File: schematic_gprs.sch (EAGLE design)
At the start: 46 parts, among them J1 Jumper Alimentaciones, Q1 MOSFET-NCHANNEL2N7000, Q2 MOSFET-NCHANNEL2N7000, T1 BC547, X1 LTI-SASF54GT

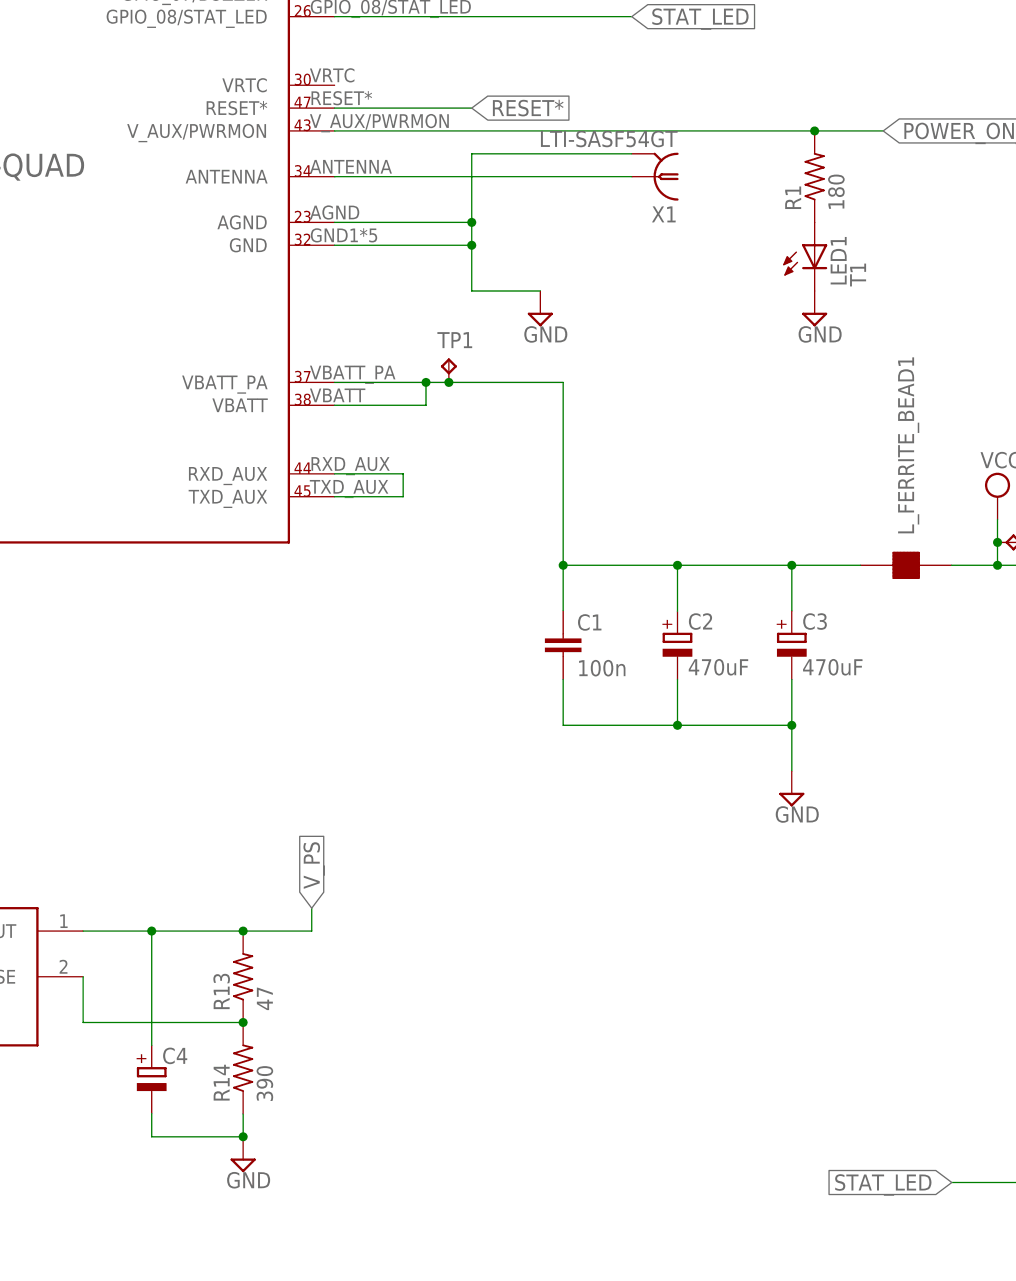
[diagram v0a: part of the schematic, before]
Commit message: Pistas realizadas
Se acaban todas las conexiones restantes. Se replantean los valores de
las resistencias para el led y se modifican también los valores de las
resistencias a la salida del regulador de tensión. Se añade un
condensador de 1uF a la entrada de VCC de la tarjeta SIM:
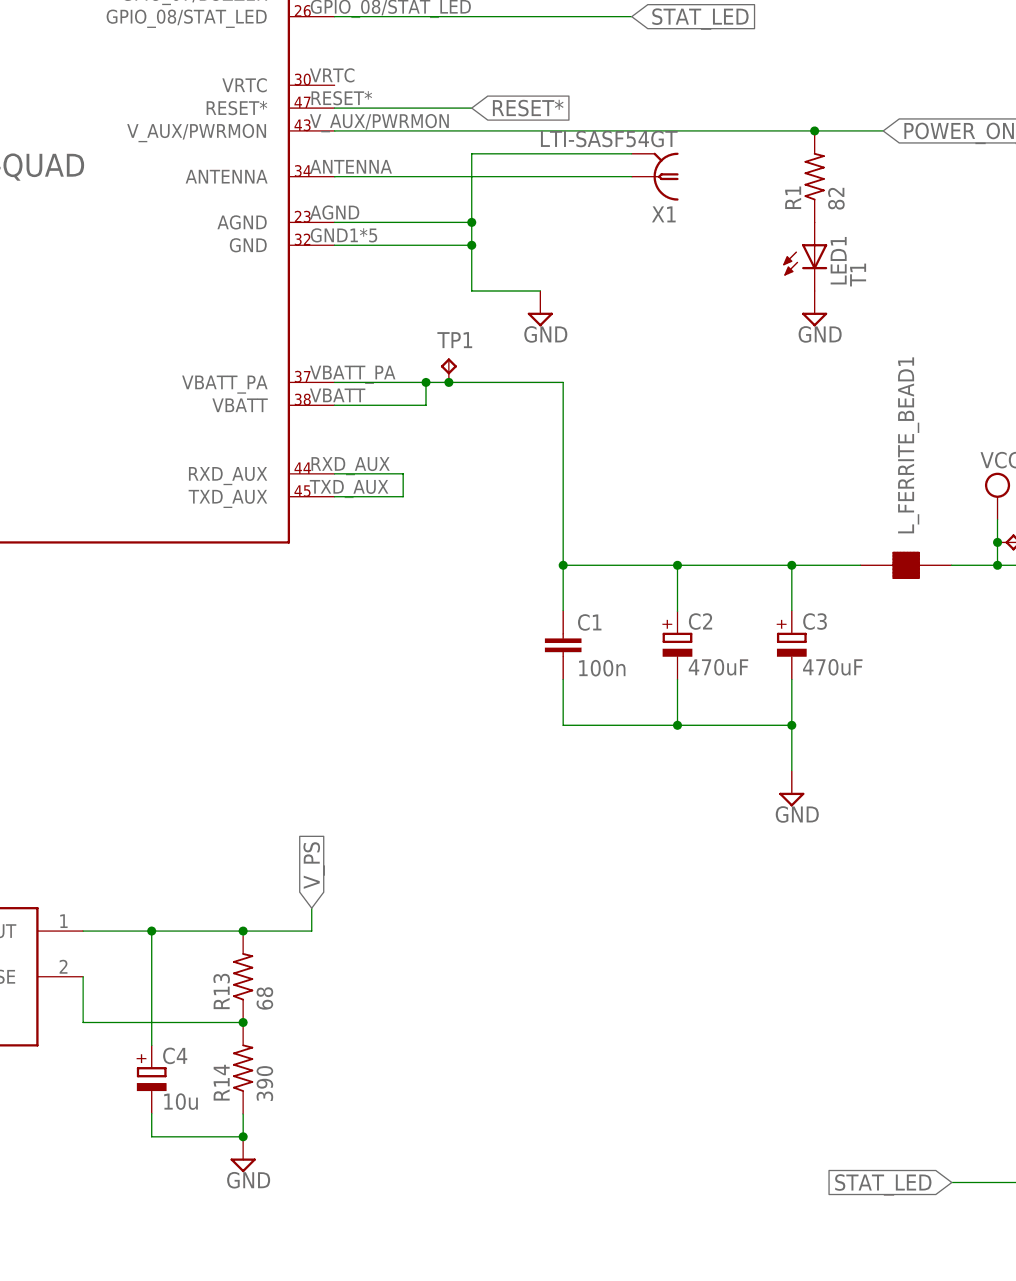
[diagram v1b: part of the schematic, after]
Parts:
- C4: value (none) -> 10u
- R1: value 180 -> 82
- R13: value 47 -> 68
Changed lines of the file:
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@@
 <part name="LED1" library="led" deviceset="LED" device="3MM" value="T1"/>
 <part name="SUPPLY10" library="supply2" deviceset="GND" device=""/>
-<part name="R1" library="resistor" deviceset="R-US_" device="0207/7" value="180"/>
+<part name="R1" library="resistor" deviceset="R-US_" device="0207/7" value="82"/>
 <part name="R3" library="resistor" deviceset="R-US_" device="0207/7" value="180"/>
 <part name="LED2" library="led" deviceset="LED" device="3MM" value="T1"/>
@@
 <part name="J1" library="jumper" deviceset="J2" device="X2MM" value="Jumper Alimentaciones"/>
 <part name="L_FERRITE_BEAD1" library="sym" deviceset="FERRITEBEAD2" device=""/>
-<part name="R13" library="resistor" deviceset="R-US_" device="0207/7" value="47"/>
-<part name="C4" library="resistor" deviceset="CPOL-EU" device="E2-5"/>
+<part name="R13" library="resistor" deviceset="R-US_" device="0207/7" value="68"/>
+<part name="C4" library="resistor" deviceset="CPOL-EU" device="E2-5" value="10u"/>
 <part name="R14" library="resistor" deviceset="R-US_" device="0207/7" value="390"/>
 <part name="SUPPLY7" library="supply2" deviceset="GND" device=""/>
